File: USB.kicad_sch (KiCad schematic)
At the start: 7 parts, among them J2 USB_C_Receptacle_USB2.0_16P, U1 USBLC6-2SC6, U2 NCP1117-3.3_SOT223

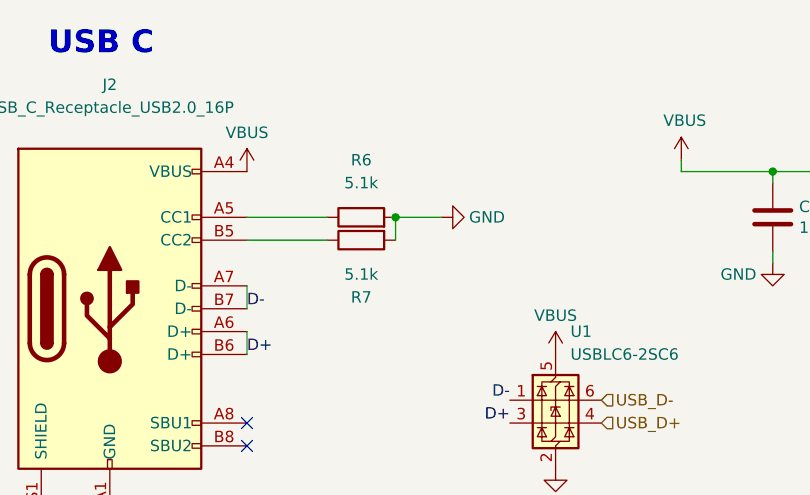
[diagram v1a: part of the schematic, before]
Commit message: routing, rotate leds to make tracks easier
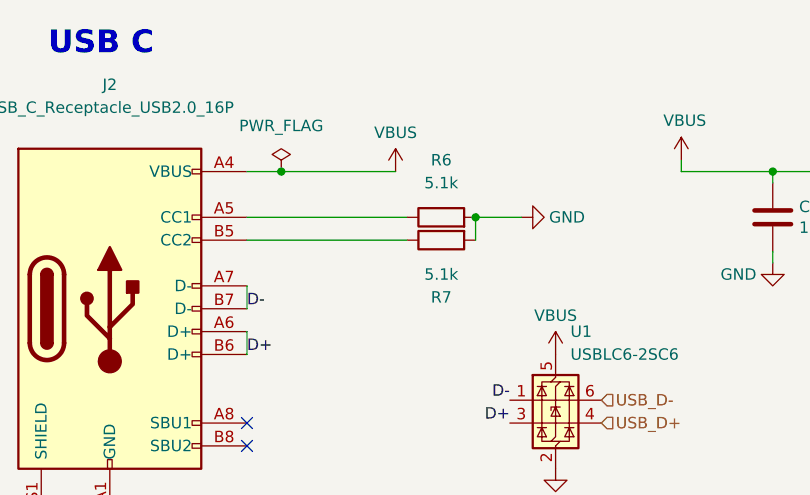
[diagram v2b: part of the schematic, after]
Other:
- moved on the sheet: R6, R7

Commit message: add part nums for bom
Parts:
- C1, C2: LCSC (none) -> C15850; MPN (none) -> CL21A106KAYNNNE; Manufacturer (none) -> Samsung Electro-Mechanics; Type (none) -> SMD
- J2: Comment (none) -> Do Not Substitute; LCSC (none) -> C165948; MPN (none) -> TYPE-C-31-M-12; Manufacturer (none) -> Korean Hroparts Elec; Type (none) -> THRU-HOLE
- R6, R7: LCSC (none) -> C25905; MPN (none) -> 0402WGF5101TCE; Manufacturer (none) -> UNIROYAL; Type (none) -> SMD
- U1: LCSC (none) -> C7519; MPN (none) -> USBLC6-2SC6; Manufacturer (none) -> MSKSEMI; Type (none) -> SMD
- U2: value NCP1117-3.3_SOT223 -> NCP1117ST33T3G; LCSC (none) -> C26537; MPN (none) -> NCP1117ST33T3G; Manufacturer (none) -> onsemi; Type (none) -> SMD

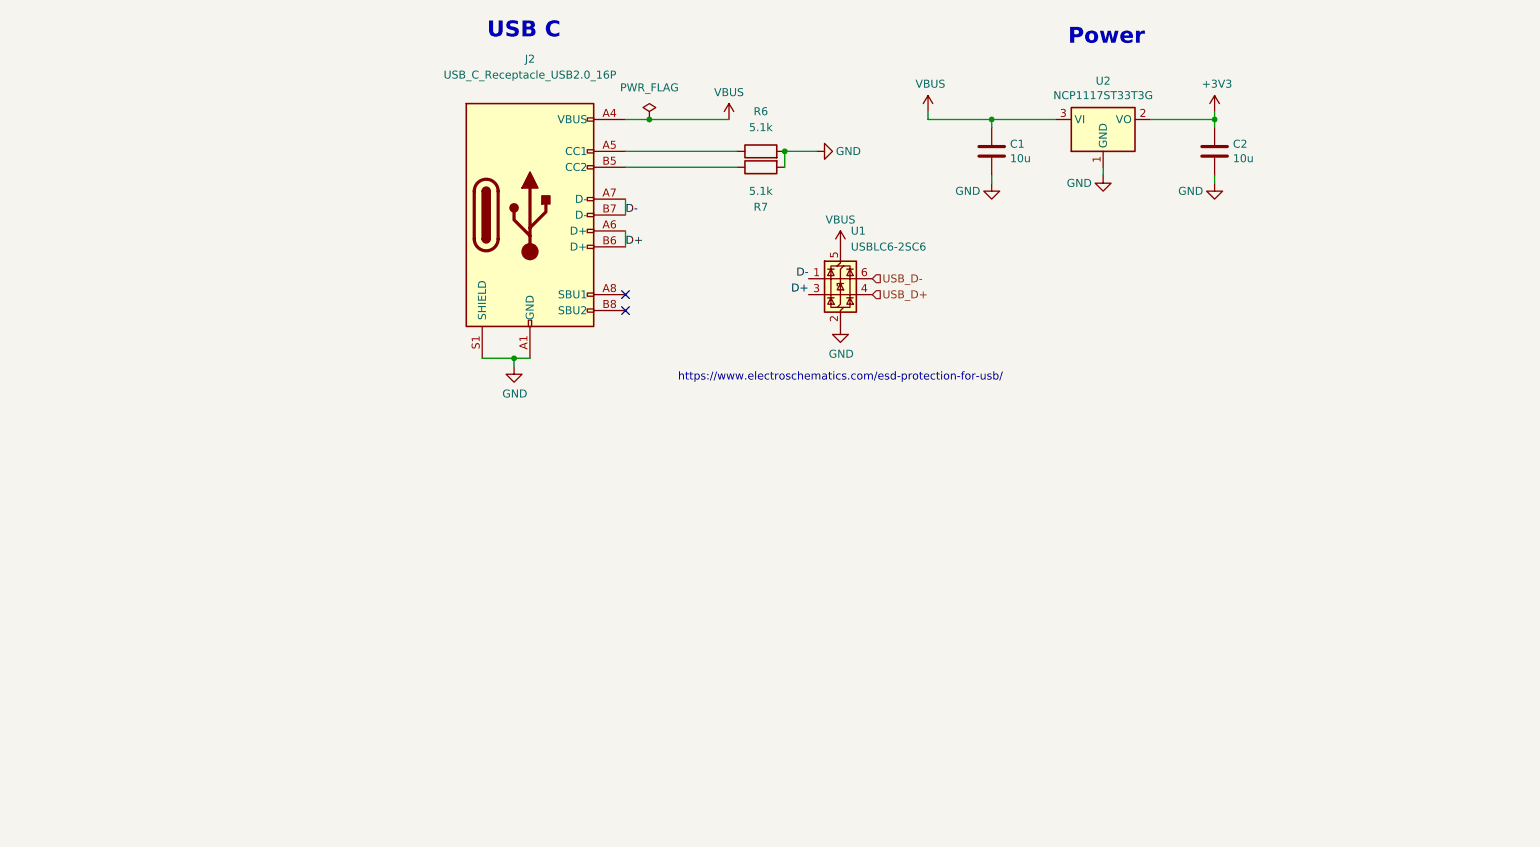
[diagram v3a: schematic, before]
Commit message: usb changes for high power (leds)
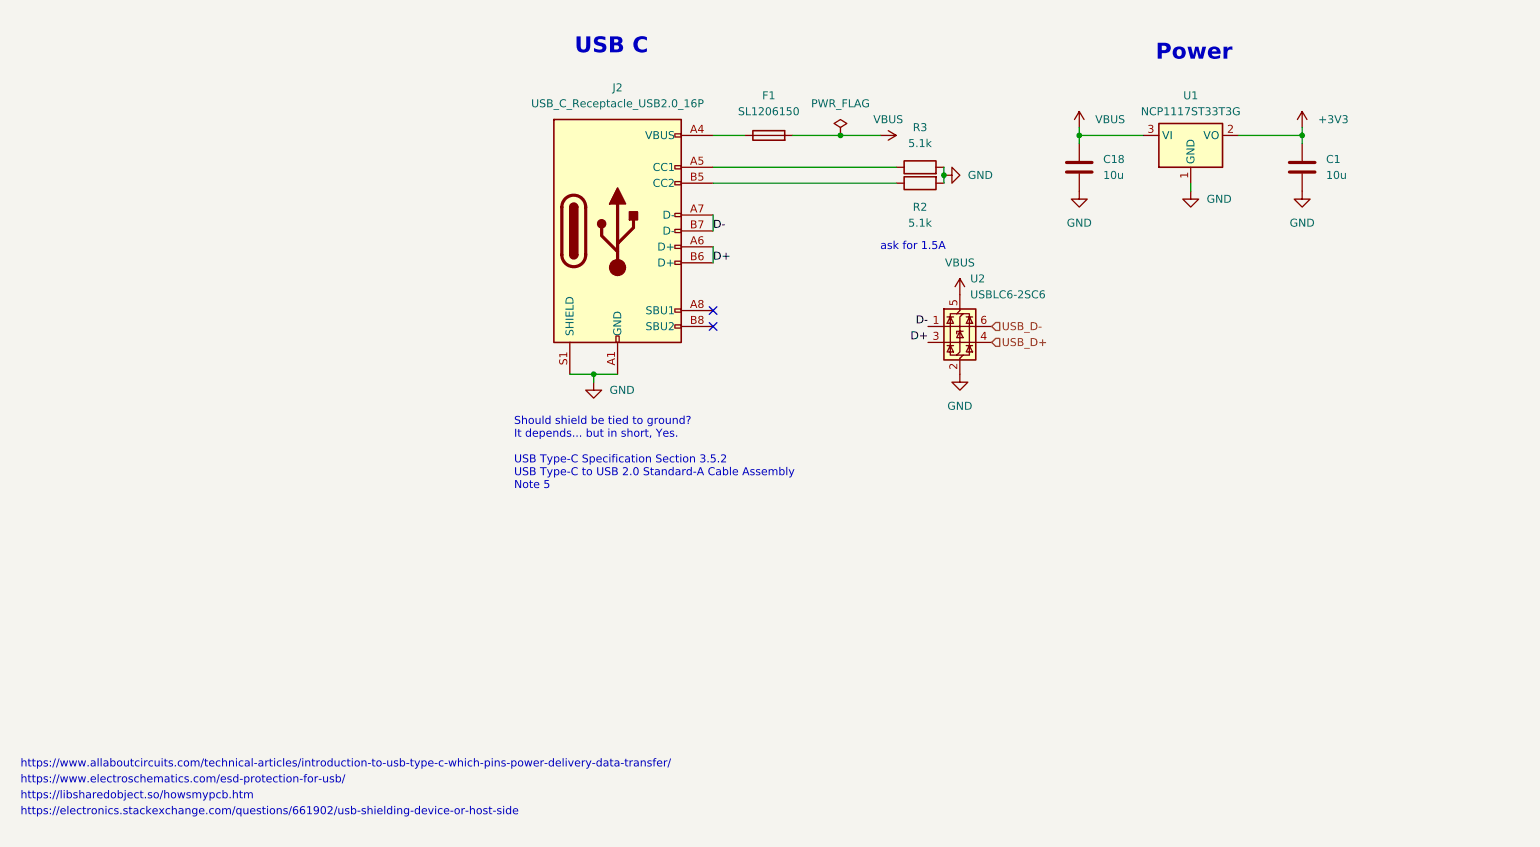
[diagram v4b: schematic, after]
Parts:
- added F1: SL1206150, Fuse:Fuse_1206_3216Metric_Pad1.42x1.75mm_HandSolder, symbol Device:Fuse
- renumbered C2 to C1, C1 to C18, R7 to R2, R6 to R3, U2 to U1, U1 to U2
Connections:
- net VBUS: now also F1.2; no longer J2.A4 (VBUS), J2.A9 (VBUS), J2.B4 (VBUS), J2.B9 (VBUS)
- new net: F1.1, J2.A4 (VBUS), J2.A9 (VBUS), J2.B4 (VBUS), J2.B9 (VBUS)
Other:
- note added: "Should shield be tied to ground? It depends... but in short, Yes. USB Type-C Specification Section 3.5.2 USB Type-C to USB 2.0 Standard-A Cable Assembly Note 5"
- note added: "ask for 1.5A"
- note added: "https://electronics.stackexchange.com/questions/661902/usb-shielding-device-or-host-side"
- note added: "https://libsharedobject.so/howsmypcb.htm"
- note added: "https://www.allaboutcircuits.com/technical-articles/introduction-to-usb-type-c-which-pins-power-delivery-data-transfer/"
- title: (none) -> USB Connector and 3V3 Supply + Protections
- moved on the sheet: C1, C18, J2, R2, R3, U1, U2

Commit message: bulk cap and level shifter (still need to lay out)
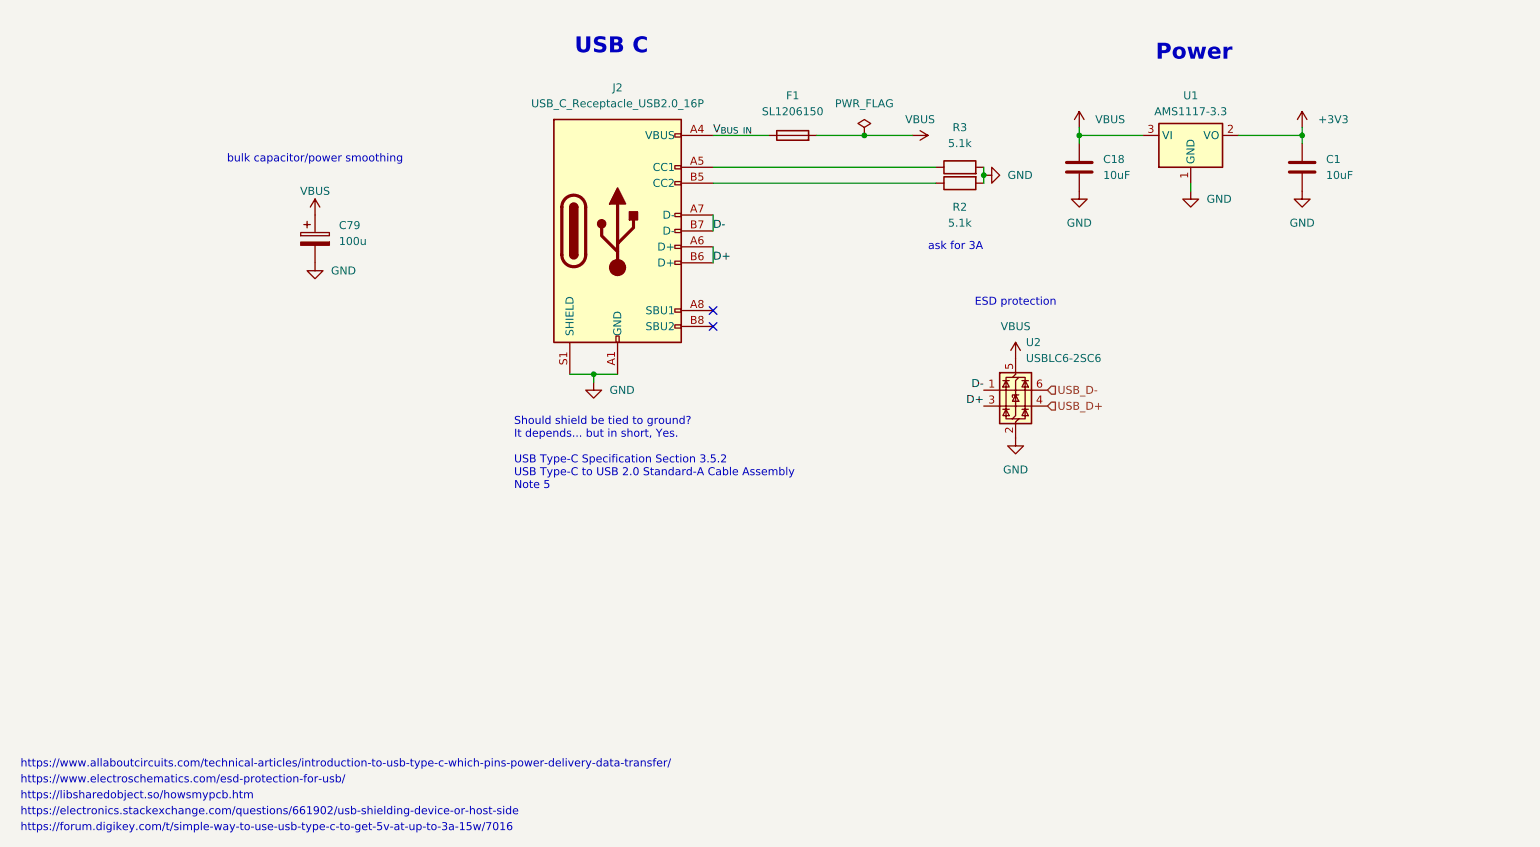
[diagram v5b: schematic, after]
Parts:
- added C79: 100u, Capacitor_SMD:CP_Elec_6.3x5.4, symbol Device:C_Polarized
- C1, C18: value 10u -> 10uF
- U1: value NCP1117ST33T3G -> AMS1117-3.3; symbol Regulator_Linear:NCP1117-3.3_SOT223 -> Regulator_Linear:AMS1117-3.3; LCSC C26537 -> C6186; MPN NCP1117ST33T3G -> AMS1117-3.3; Manufacturer onsemi -> Advanced Monolithic Systems
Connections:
- net GND: now also C79.2
- net VBUS: now also C79.1
- net V_{BUS_IN}: now reaches F1.1, J2.A4 (VBUS), J2.A9 (VBUS), J2.B4 (VBUS), J2.B9 (VBUS)
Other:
- note added: "ESD protection"
- note added: "ask for 3A"
- note added: "bulk capacitor/power smoothing"
- note added: "https://forum.digikey.com/t/simple-way-to-use-usb-type-c-to-get-5v-at-up-to-3a-15w/7016"
- note removed: "ask for 1.5A"
- moved on the sheet: F1, R2, R3, U2

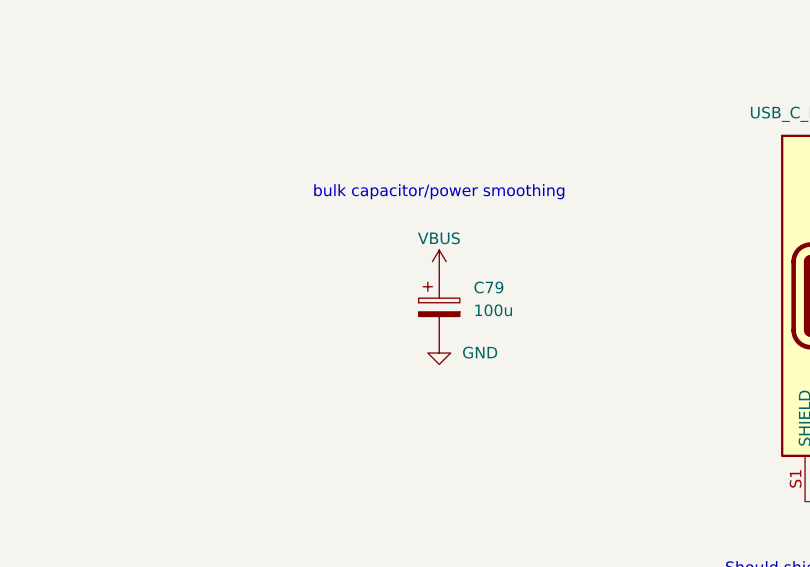
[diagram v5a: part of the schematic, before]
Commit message: bulk caps for power (todo, split 470uF cap so that it can be shorter)
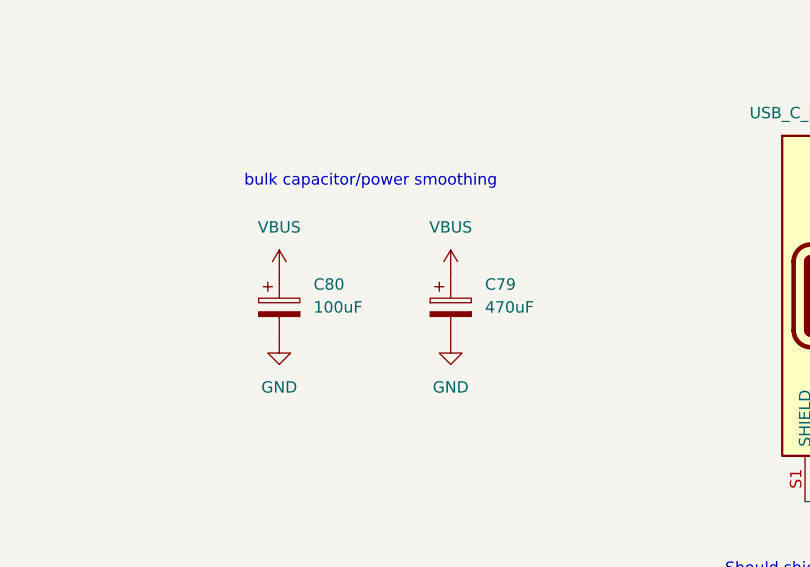
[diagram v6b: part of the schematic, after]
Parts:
- added C80: 100uF, Capacitor_SMD:CP_Elec_6.3x4.5, symbol Device:C_Polarized
- C79: value 100u -> 470uF; footprint Capacitor_SMD:CP_Elec_6.3x5.4 -> Capacitor_SMD:CP_Elec_8x10; LCSC C128530 -> C134739; MPN EEE1CA101WP -> VE-471M0JTR-0810; Manufacturer Panasonic -> Lelon
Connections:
- net GND: now also C80.2
- net VBUS: now also C80.1

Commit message: add debug led, make bulk caps smaller, export plate and bottom for rudimentary case
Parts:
- added C86, C87: 100uF, Capacitor_SMD:C_1206_3216Metric, symbol Device:C_Polarized
- C79: value 470uF -> 100uF; footprint Capacitor_SMD:CP_Elec_8x10 -> Capacitor_SMD:C_1206_3216Metric; LCSC C134739 -> C15008; MPN VE-471M0JTR-0810 -> CL31A107MQHNNNE; Manufacturer Lelon -> Samsung Electro-Mechanics
- C80: footprint Capacitor_SMD:CP_Elec_6.3x4.5 -> Capacitor_SMD:C_1206_3216Metric; LCSC C22388021 -> C15008; MPN EFVM025ADA101M0654 -> CL31A107MQHNNNE; Manufacturer FOLLON -> Samsung Electro-Mechanics
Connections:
- net GND: now also C86.2, C87.2
- net VBUS: now also C86.1, C87.1
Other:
- moved on the sheet: C80

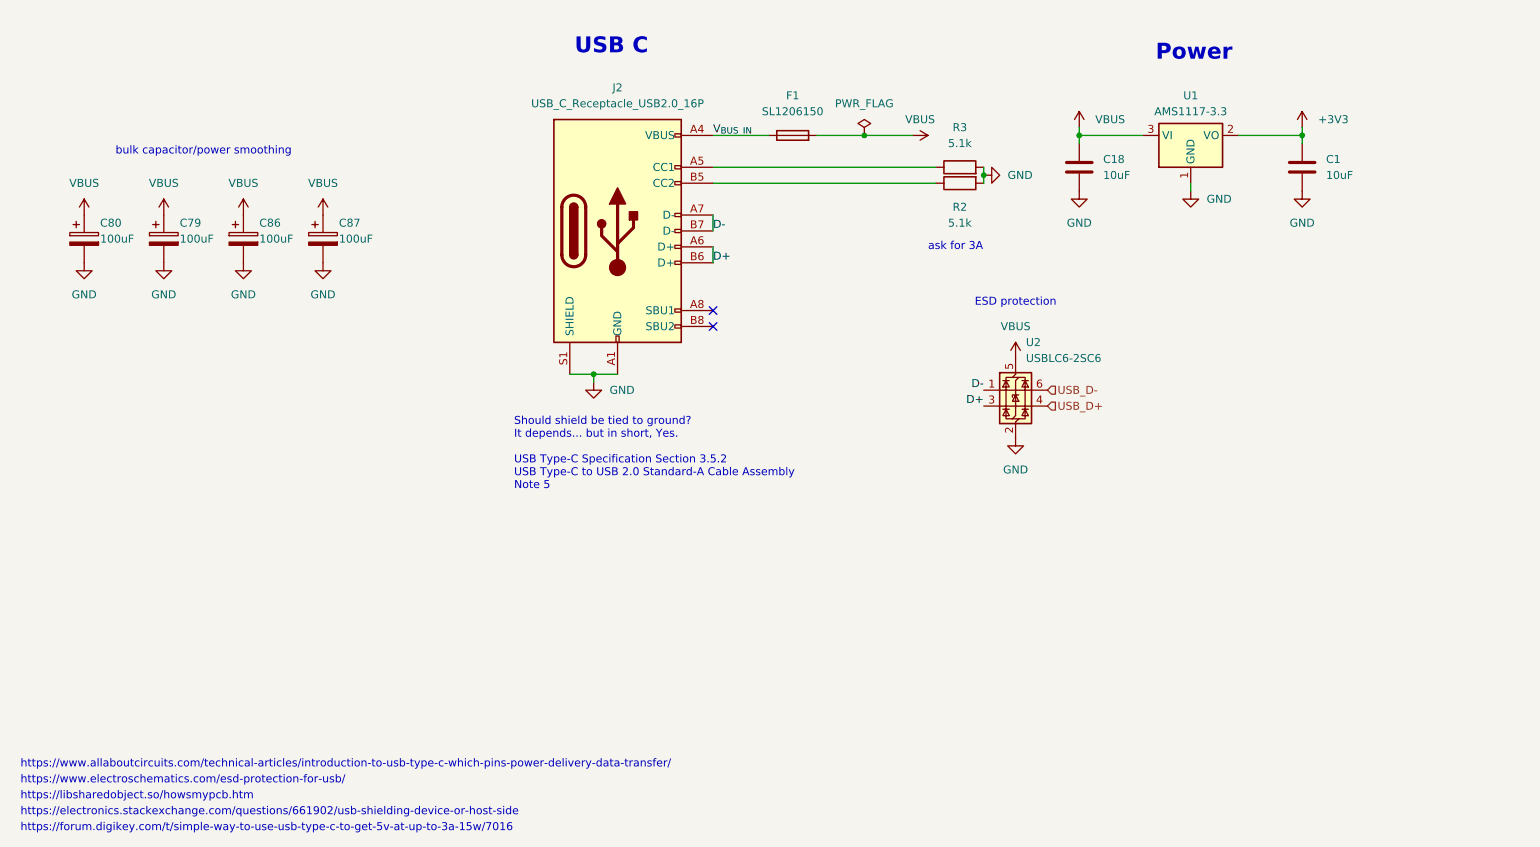
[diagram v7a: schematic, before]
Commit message: enlarge mounting holes, custom rules
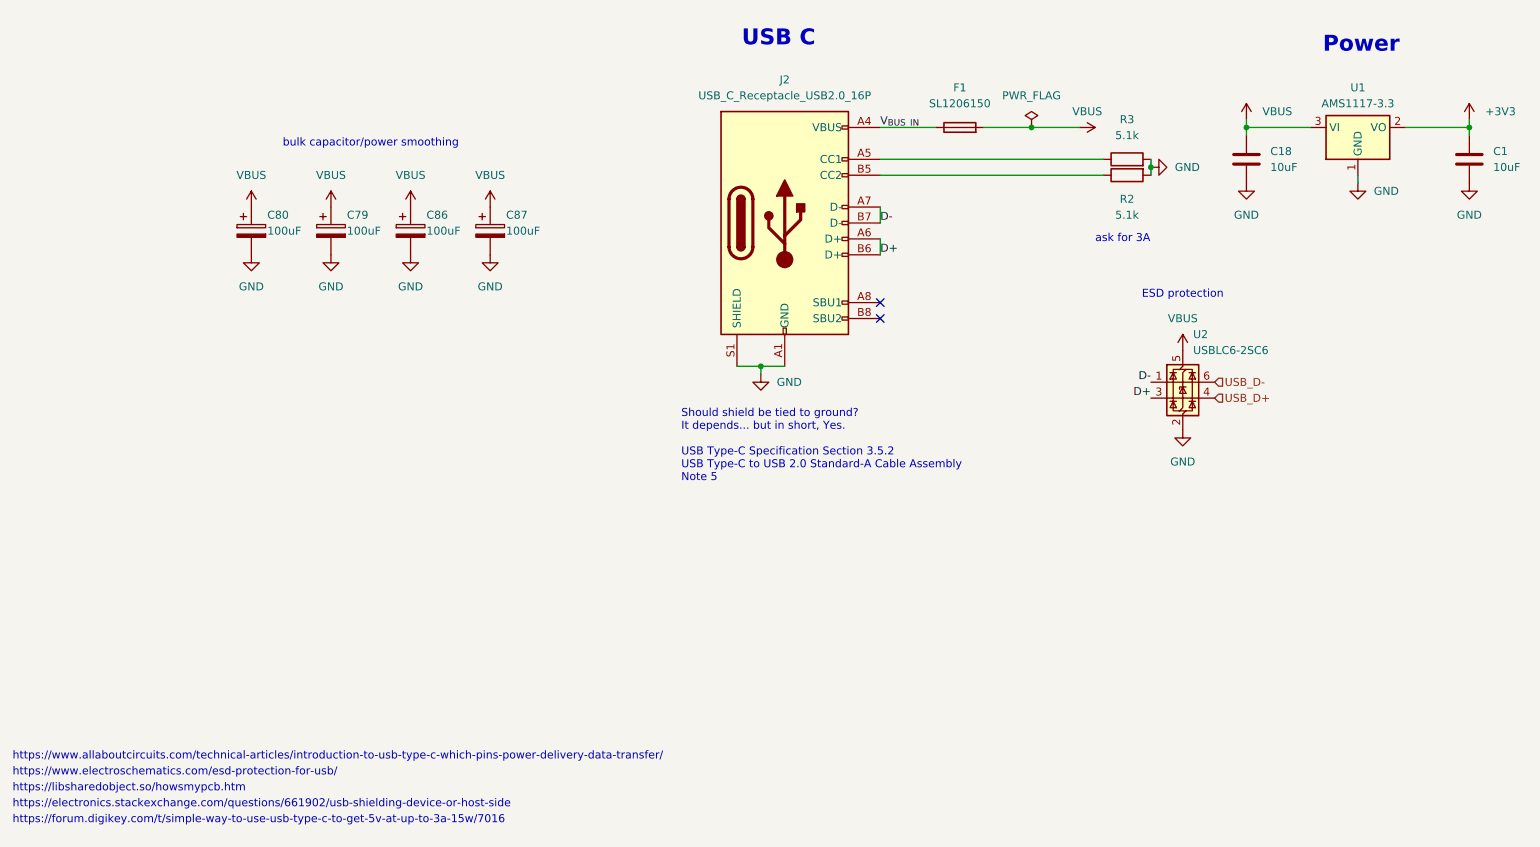
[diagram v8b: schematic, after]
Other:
- moved on the sheet: C1, C18, C79, C80, C86, C87, F1, J2, R2, R3, U1, U2
